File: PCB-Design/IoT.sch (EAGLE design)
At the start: 11 parts, among them M2 ARDUINO-NANO-3.0, M3 WIRELESS-NRF24L01

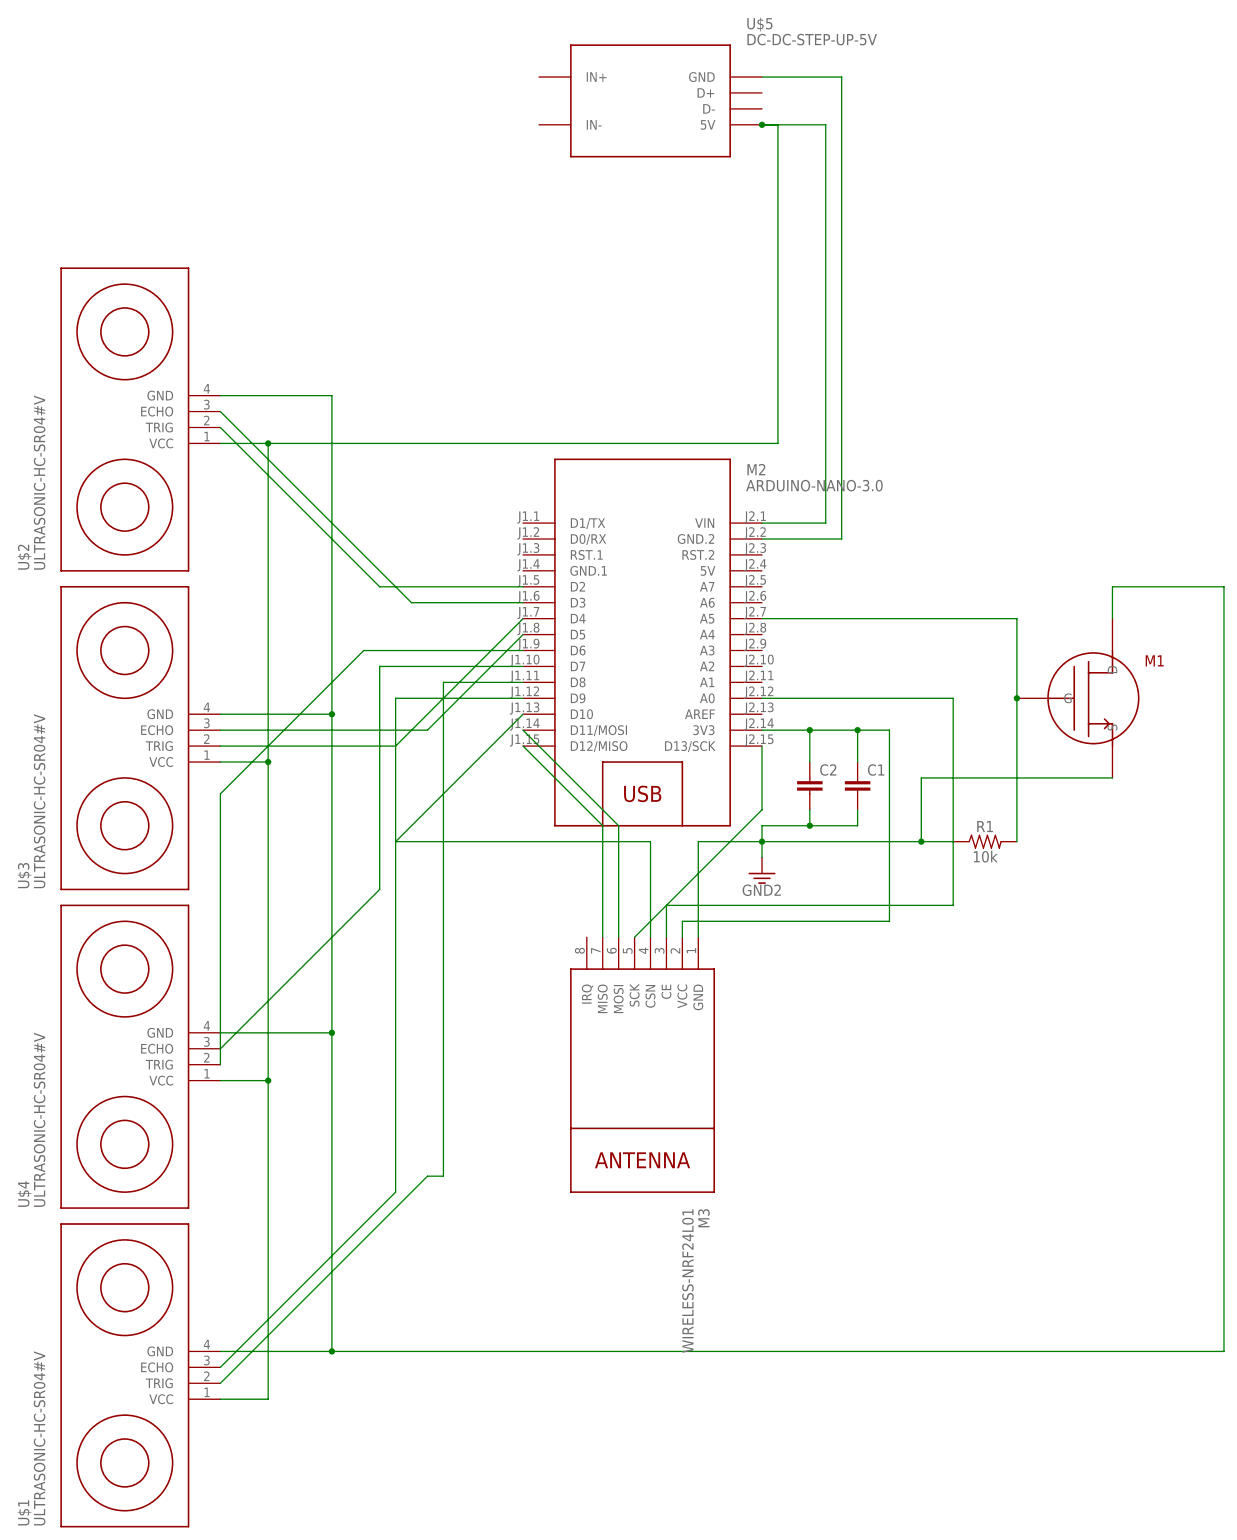
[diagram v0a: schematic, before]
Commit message: schematic - fixed mosfet and tidy up, board - manually routed (auto route super scary results)
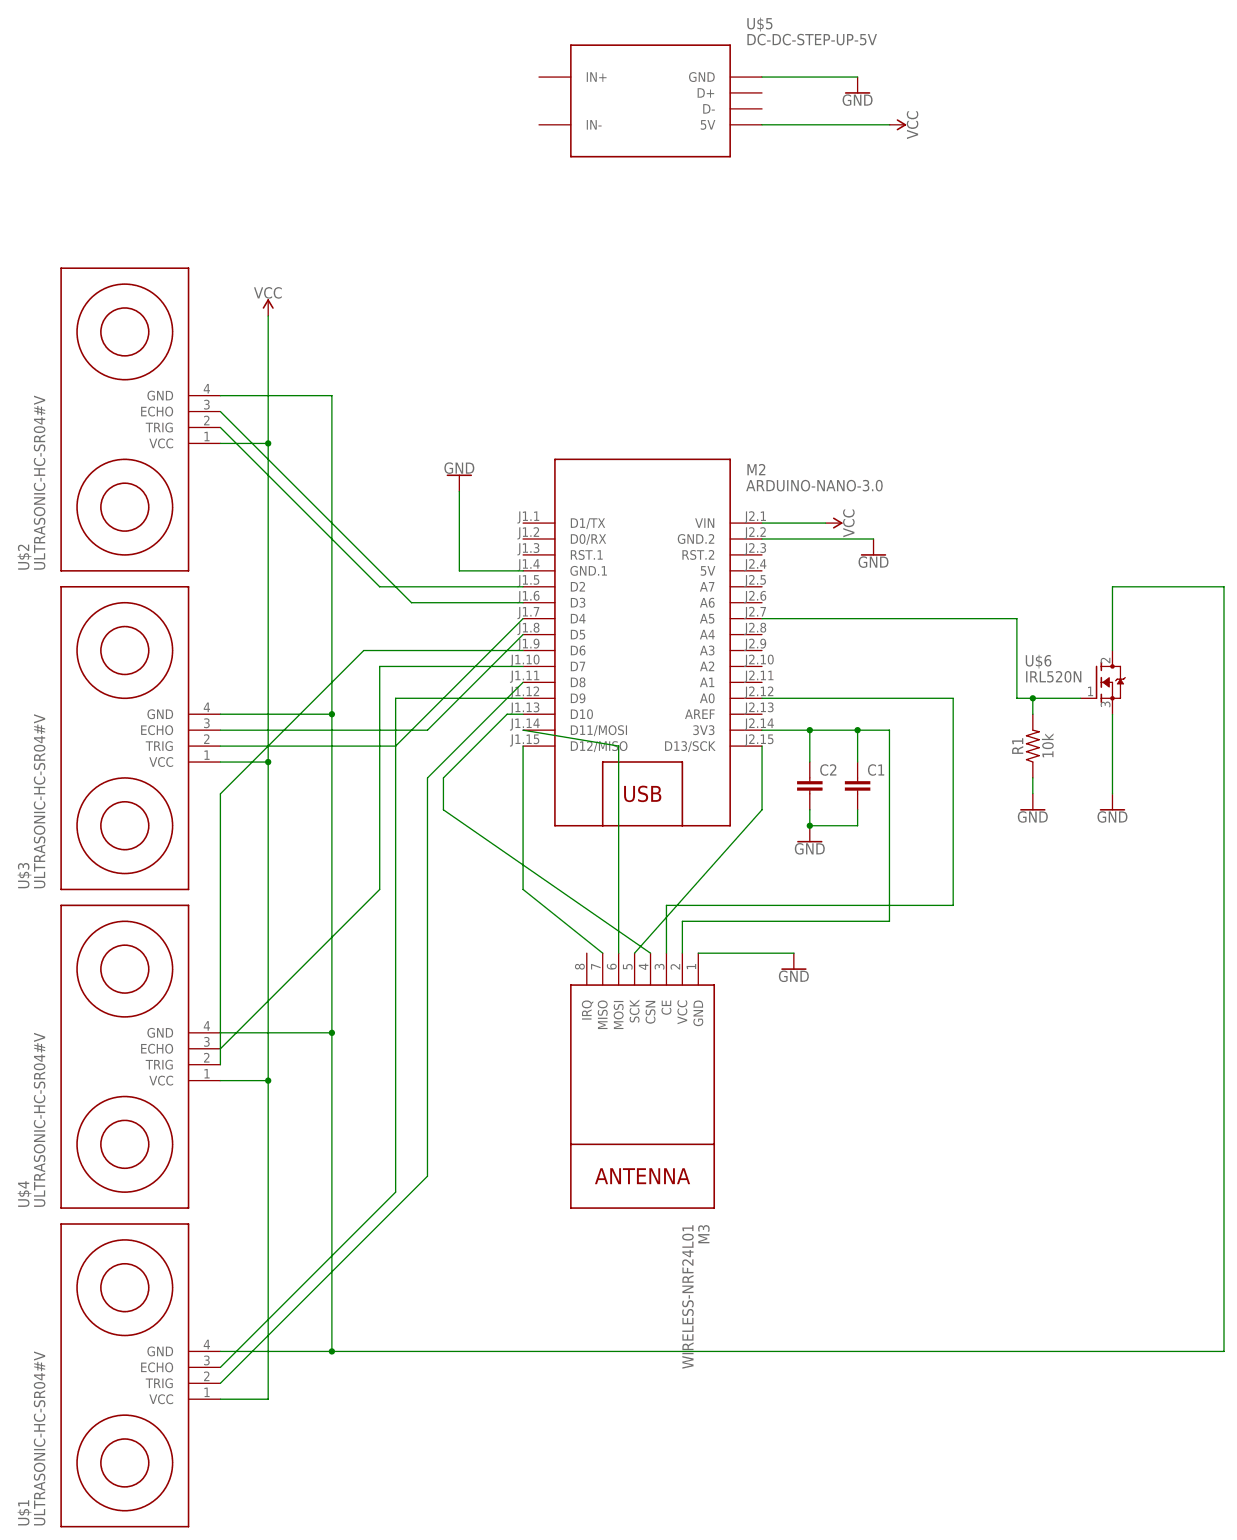
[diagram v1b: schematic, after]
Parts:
- removed M1: (no value), ngspice-simulation:FET_N
- added U$6: IRL520N, IRL520N:IRL520N
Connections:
- net N$19 renamed VCC
- removed net 3.3V: C1.2, C2.2, M1.S, M3.GND, R1.1
- removed net N$2: M2.GND.2, U$5.GND
- new net GND: C1.2, C2.2, M2.GND.1, M2.GND.2, M3.GND, R1.1, U$5.GND, U$6.S
- net N$1: now also U$6.G; no longer M1.G
- net N$9: now also U$6.D; no longer M1.D
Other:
- moved on the sheet: M3, R1

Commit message: updated names on board
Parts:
- renumbered U$1 to HC-SR04-4, U$2 to HC-SR04-1, U$3 to HC-SR04-2, U$4 to HC-SR04-3
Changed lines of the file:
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@@
 <part name="M2" library="diy-modules" deviceset="ARDUINO-NANO-3.0" device=""/>
 <part name="R1" library="SparkFun-Resistors" library_urn="urn:adsk.eagle:library:532" deviceset="10KOHM" device="-HORIZ_KIT-1/4W-1%" package3d_urn="urn:adsk.eagle:package:39661/1" value="10k"/>
-<part name="U$1" library="diy-modules" deviceset="ULTRASONIC-HC-SR04" device="#V"/>
-<part name="U$2" library="diy-modules" deviceset="ULTRASONIC-HC-SR04" device="#V"/>
-<part name="U$3" library="diy-modules" deviceset="ULTRASONIC-HC-SR04" device="#V"/>
-<part name="U$4" library="diy-modules" deviceset="ULTRASONIC-HC-SR04" device="#V"/>
+<part name="HC-SR04-4" library="diy-modules" deviceset="ULTRASONIC-HC-SR04" device="#V"/>
+<part name="HC-SR04-1" library="diy-modules" deviceset="ULTRASONIC-HC-SR04" device="#V"/>
+<part name="HC-SR04-2" library="diy-modules" deviceset="ULTRASONIC-HC-SR04" device="#V"/>
+<part name="HC-SR04-3" library="diy-modules" deviceset="ULTRASONIC-HC-SR04" device="#V"/>
 <part name="U$5" library="diy-modules" deviceset="DC-DC-STEP-UP-5V" device=""/>
 <part name="C1" library="resistor" library_urn="urn:adsk.eagle:library:348" deviceset="C-EU" device="025-040X050" package3d_urn="urn:adsk.eagle:package:26150/1"/>
@@
 <instance part="M2" gate="G$1" x="27.94" y="30.48"/>
 <instance part="R1" gate="G$1" x="88.9" y="12.7" rot="R90"/>
-<instance part="U$1" gate="G$1" x="-55.88" y="-88.9" rot="R90"/>
-<instance part="U$2" gate="G$1" x="-55.88" y="63.5" rot="R90"/>
-<instance part="U$3" gate="G$1" x="-55.88" y="12.7" rot="R90"/>
-<instance part="U$4" gate="G$1" x="-55.88" y="-38.1" rot="R90"/>
+<instance part="HC-SR04-4" gate="G$1" x="-55.88" y="-88.9" rot="R90"/>
+<instance part="HC-SR04-1" gate="G$1" x="-55.88" y="63.5" rot="R90"/>
+<instance part="HC-SR04-2" gate="G$1" x="-55.88" y="12.7" rot="R90"/>
+<instance part="HC-SR04-3" gate="G$1" x="-55.88" y="-38.1" rot="R90"/>
 <instance part="U$5" gate="G$1" x="27.94" y="114.3"/>
 <instance part="C1" gate="G$1" x="60.96" y="7.62"/>
@@
 <net name="N$9" class="0">
 <segment>
-<pinref part="U$1" gate="G$1" pin="GND"/>
+<pinref part="HC-SR04-4" gate="G$1" pin="GND"/>
 <wire x1="-40.64" y1="-83.82" x2="-22.86" y2="-83.82" width="0.1524" layer="91"/>
 <wire x1="-22.86" y1="-83.82" x2="119.38" y2="-83.82" width="0.1524" layer="91"/>
 <wire x1="119.38" y1="-83.82" x2="119.38" y2="38.1" width="0.1524" layer="91"/>
 <wire x1="119.38" y1="38.1" x2="101.6" y2="38.1" width="0.1524" layer="91"/>
-<pinref part="U$4" gate="G$1" pin="GND"/>
+<pinref part="HC-SR04-3" gate="G$1" pin="GND"/>
 <wire x1="-40.64" y1="-33.02" x2="-22.86" y2="-33.02" width="0.1524" layer="91"/>
 <wire x1="-22.86" y1="-33.02" x2="-22.86" y2="-83.82" width="0.1524" layer="91"/>
 <junction x="-22.86" y="-83.82"/>
-<pinref part="U$3" gate="G$1" pin="GND"/>
+<pinref part="HC-SR04-2" gate="G$1" pin="GND"/>
 <wire x1="-40.64" y1="17.78" x2="-22.86" y2="17.78" width="0.1524" layer="91"/>
 <wire x1="-22.86" y1="17.78" x2="-22.86" y2="-33.02" width="0.1524" layer="91"/>
 <junction x="-22.86" y="-33.02"/>
-<pinref part="U$2" gate="G$1" pin="GND"/>
+<pinref part="HC-SR04-1" gate="G$1" pin="GND"/>
 <wire x1="-40.64" y1="68.58" x2="-22.86" y2="68.58" width="0.1524" layer="91"/>
 <wire x1="-22.86" y1="68.58" x2="-22.86" y2="17.78" width="0.1524" layer="91"/>
@@
 <net name="N$5" class="0">
 <segment>
-<pinref part="U$2" gate="G$1" pin="TRIG"/>
+<pinref part="HC-SR04-1" gate="G$1" pin="TRIG"/>
 <pinref part="M2" gate="G$1" pin="D2"/>
 <wire x1="-40.64" y1="63.5" x2="-15.24" y2="38.1" width="0.1524" layer="91"/>
@@
 <net name="N$6" class="0">
 <segment>
-<pinref part="U$2" gate="G$1" pin="ECHO"/>
+<pinref part="HC-SR04-1" gate="G$1" pin="ECHO"/>
 <pinref part="M2" gate="G$1" pin="D3"/>
 <wire x1="-40.64" y1="66.04" x2="-10.16" y2="35.56" width="0.1524" layer="91"/>
@@
 <net name="N$7" class="0">
 <segment>
-<pinref part="U$3" gate="G$1" pin="ECHO"/>
+<pinref part="HC-SR04-2" gate="G$1" pin="ECHO"/>
 <pinref part="M2" gate="G$1" pin="D5"/>
 <wire x1="-40.64" y1="15.24" x2="-7.62" y2="15.24" width="0.1524" layer="91"/>
@@
 <net name="N$8" class="0">
 <segment>
-<pinref part="U$3" gate="G$1" pin="TRIG"/>
+<pinref part="HC-SR04-2" gate="G$1" pin="TRIG"/>
 <pinref part="M2" gate="G$1" pin="D4"/>
 <wire x1="-40.64" y1="12.7" x2="-12.7" y2="12.7" width="0.1524" layer="91"/>
@@
 <net name="N$10" class="0">
 <segment>
-<pinref part="U$4" gate="G$1" pin="ECHO"/>
+<pinref part="HC-SR04-3" gate="G$1" pin="ECHO"/>
 <wire x1="-40.64" y1="-35.56" x2="-15.24" y2="-10.16" width="0.1524" layer="91"/>
 <wire x1="-15.24" y1="-10.16" x2="-15.24" y2="25.4" width="0.1524" layer="91"/>
@@
 <net name="N$11" class="0">
 <segment>
-<pinref part="U$4" gate="G$1" pin="TRIG"/>
+<pinref part="HC-SR04-3" gate="G$1" pin="TRIG"/>
 <wire x1="-40.64" y1="-38.1" x2="-40.64" y2="5.08" width="0.1524" layer="91"/>
 <wire x1="-40.64" y1="5.08" x2="-17.78" y2="27.94" width="0.1524" layer="91"/>
@@
 <net name="N$12" class="0">
 <segment>
-<pinref part="U$1" gate="G$1" pin="ECHO"/>
+<pinref part="HC-SR04-4" gate="G$1" pin="ECHO"/>
 <wire x1="-40.64" y1="-86.36" x2="-12.7" y2="-58.42" width="0.1524" layer="91"/>
 <wire x1="-12.7" y1="-58.42" x2="-12.7" y2="20.32" width="0.1524" layer="91"/>
@@
 <net name="N$13" class="0">
 <segment>
-<pinref part="U$1" gate="G$1" pin="TRIG"/>
+<pinref part="HC-SR04-4" gate="G$1" pin="TRIG"/>
 <wire x1="-40.64" y1="-88.9" x2="-7.62" y2="-55.88" width="0.1524" layer="91"/>
 <wire x1="-7.62" y1="-55.88" x2="-7.62" y2="7.62" width="0.1524" layer="91"/>
@@
 </segment>
 <segment>
-<pinref part="U$2" gate="G$1" pin="VCC"/>
-<pinref part="U$3" gate="G$1" pin="VCC"/>
+<pinref part="HC-SR04-1" gate="G$1" pin="VCC"/>
+<pinref part="HC-SR04-2" gate="G$1" pin="VCC"/>
 <wire x1="-33.02" y1="60.96" x2="-40.64" y2="60.96" width="0.1524" layer="91"/>
 <wire x1="-40.64" y1="10.16" x2="-33.02" y2="10.16" width="0.1524" layer="91"/>
 <wire x1="-33.02" y1="10.16" x2="-33.02" y2="60.96" width="0.1524" layer="91"/>
-<pinref part="U$4" gate="G$1" pin="VCC"/>
+<pinref part="HC-SR04-3" gate="G$1" pin="VCC"/>
 <wire x1="-40.64" y1="-40.64" x2="-33.02" y2="-40.64" width="0.1524" layer="91"/>
 <wire x1="-33.02" y1="-40.64" x2="-33.02" y2="10.16" width="0.1524" layer="91"/>
 <junction x="-33.02" y="10.16"/>
-<pinref part="U$1" gate="G$1" pin="VCC"/>
+<pinref part="HC-SR04-4" gate="G$1" pin="VCC"/>
 <wire x1="-40.64" y1="-91.44" x2="-33.02" y2="-91.44" width="0.1524" layer="91"/>
 <wire x1="-33.02" y1="-91.44" x2="-33.02" y2="-40.64" width="0.1524" layer="91"/>

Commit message: Redone PCB on bottom only
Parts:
- C1, C2: value (none) -> 10U/35V; device resistor:C-EU025-040X050 -> capacitors-electrolytic:10U/35V
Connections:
- removed net N$4: C1.1, C2.1, M2.3V3, M3.VCC
- new net N$2: C1.+, C2.+, M2.3V3, M3.VCC
- net GND: now also C1.-, C2.-; no longer C1.2, C2.2
